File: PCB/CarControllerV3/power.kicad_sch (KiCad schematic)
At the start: 18 parts, among them U17 AP62200Z6-7, U5 ICL7660AIBAZA, U9 AMS1117-3.3

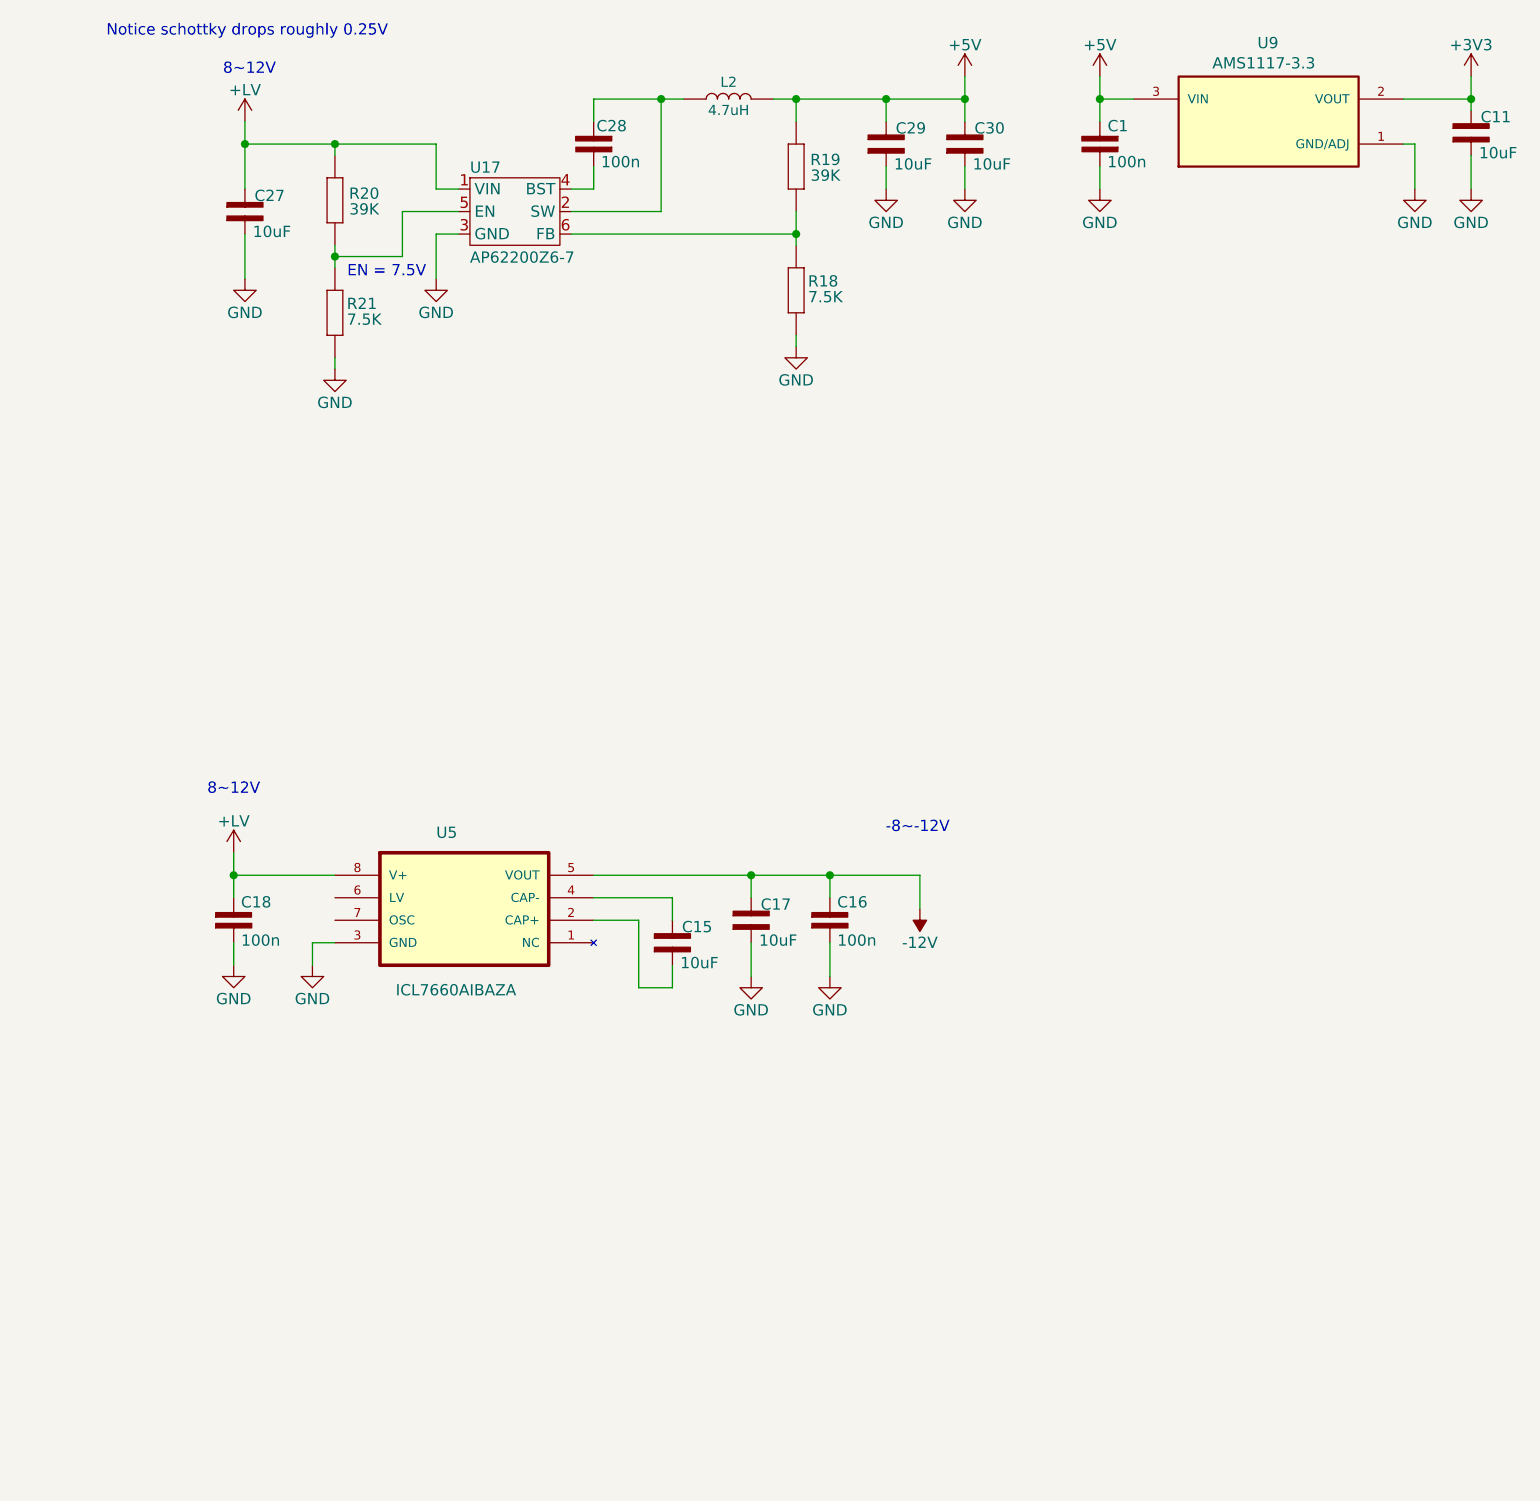
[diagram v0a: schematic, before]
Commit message: More work to PCB
- Rerouted bunch of connections
- Added alternative charge pump circuit
- Bunch of work on analog circuit
- Removed all the capacitor filter on the connectors in favor of filtering when nessesary.
- Placed canbus on JP5.2, JP5.3
- Disconnected various connections that needs to be decided if we should use.
- Added protection to various areas
- Added various todo notes everywhere..
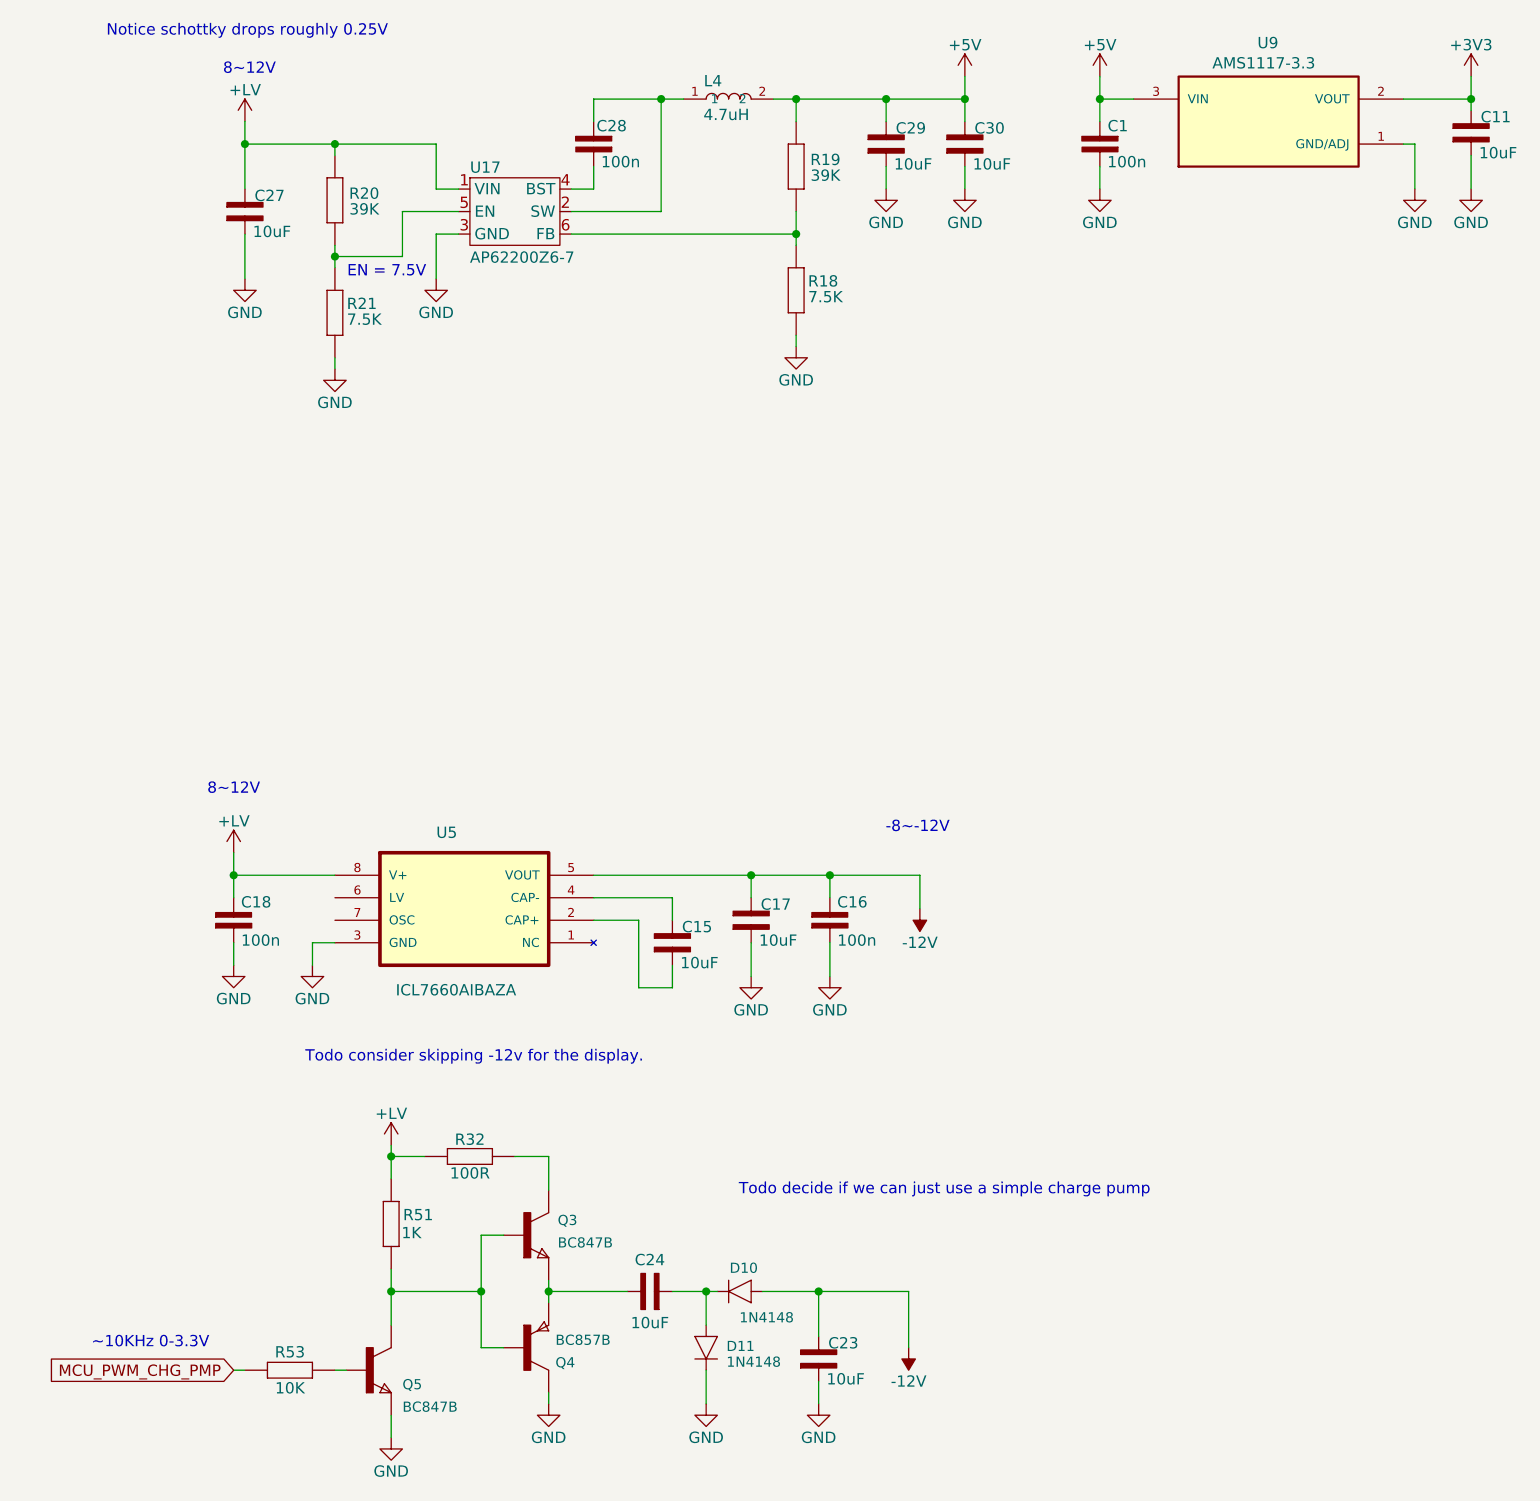
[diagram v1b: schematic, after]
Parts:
- removed L2: 4.7uH, footprints:CC0805, symbol mpl2012s4r7:MPL2012S4R7
- added C23, C24: 10uF, CC0805KKX5R8BB106:CC0805KKX5R8BB106-CAPC2013X145N, symbol CC0805KKX5R8BB106:CC0805KKX5R8BB106
- added D10, D11: 1N4148, footprints:1N4148W-7-F-SOD3715X135N, symbol 1N4148W-7-F:1N4148W-7-F
- added L4: 4.7uH, footprints:MPL-SE2512, symbol MPL-SE2512-4R7:MPL-SE2512-4R7
- added Q3, Q5: BC847B, footprints:BC847BHZGT116_SOT23, symbol BC857BHZGT116:BC847BHZGT116
- added Q4: BC857B, footprints:BC847BHZGT116_SOT23, symbol BC847B:BC857B
- added R32: 100R, footprints:RC0603FR-RESC1608X60N.pretty, symbol RC0603FR:RC0603FR-07100R
- added R51: 1K, footprints:RC0603FR-RESC1608X60N.pretty, symbol RC0603FR:RC0603FR-071KL
- added R53: 10K, RC0603FR:RC0603FR-RESC1608X60N, symbol RC0603FR:RC0603FR-0710KL
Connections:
- net +5V: now also L4.2
- net +LV: now also R32.2 (R2), R51.1 (R1)
- net -12V: now also C23.2, D10.A
- net GND: now also C23.1, D11.C, Q4.C, Q5.E
- net at C28.1 (C1), U17.2 (SW): now also L4.1
- new net: C24.1, D10.C, D11.A
- new net: Q3.B, Q4.B, Q5.C, R51.2 (R2)
- new net: C24.2, Q3.E, Q4.E
- new net: Q5.B, R53.2 (R2)
- new net: Q3.C, R32.1 (R1)
- new net MCU_PWM_CHG_PMP: R53.1 (R1)
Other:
- note added: "Todo consider skipping -12v for the display."
- note added: "Todo decide if we can just use a simple charge pump"
- note added: "~10KHz 0-3.3V"
